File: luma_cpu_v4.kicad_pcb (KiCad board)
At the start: 4 copper layers, 55.8 x 64.2 mm, 117 parts, among them J1 HDMI_A_1.4, J2 USB_C_Receptacle_PowerOnly_6P, J3 Conn_02x03_Odd_Even, J4 USB_A, Q2 DMG2301L, SW1 SW_SPDT, U1 LFE5U-xxF-xBG381I, U10 TPD1E05U06DYA, U11 W25Q128JVS, U12 USB3300-EZK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

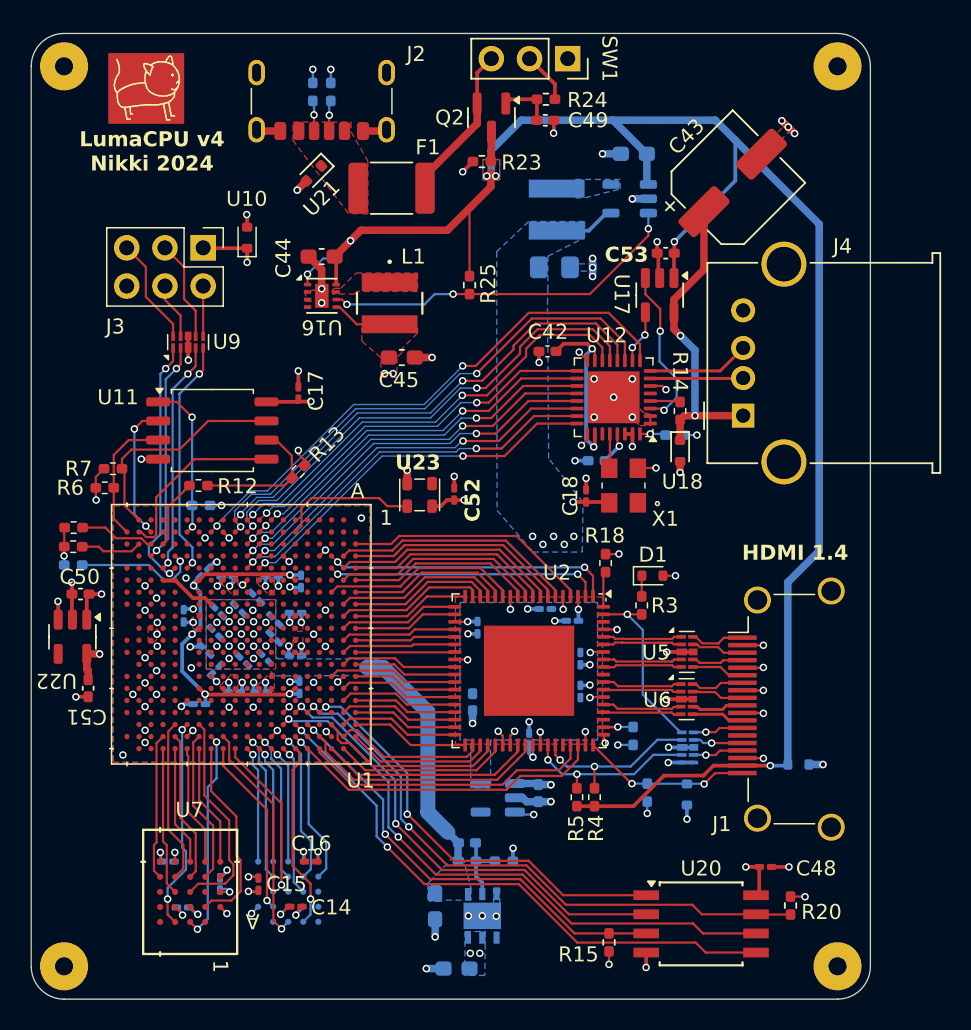
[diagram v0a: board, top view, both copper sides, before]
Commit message: added some capacitors to various components that weren't capacitored enough
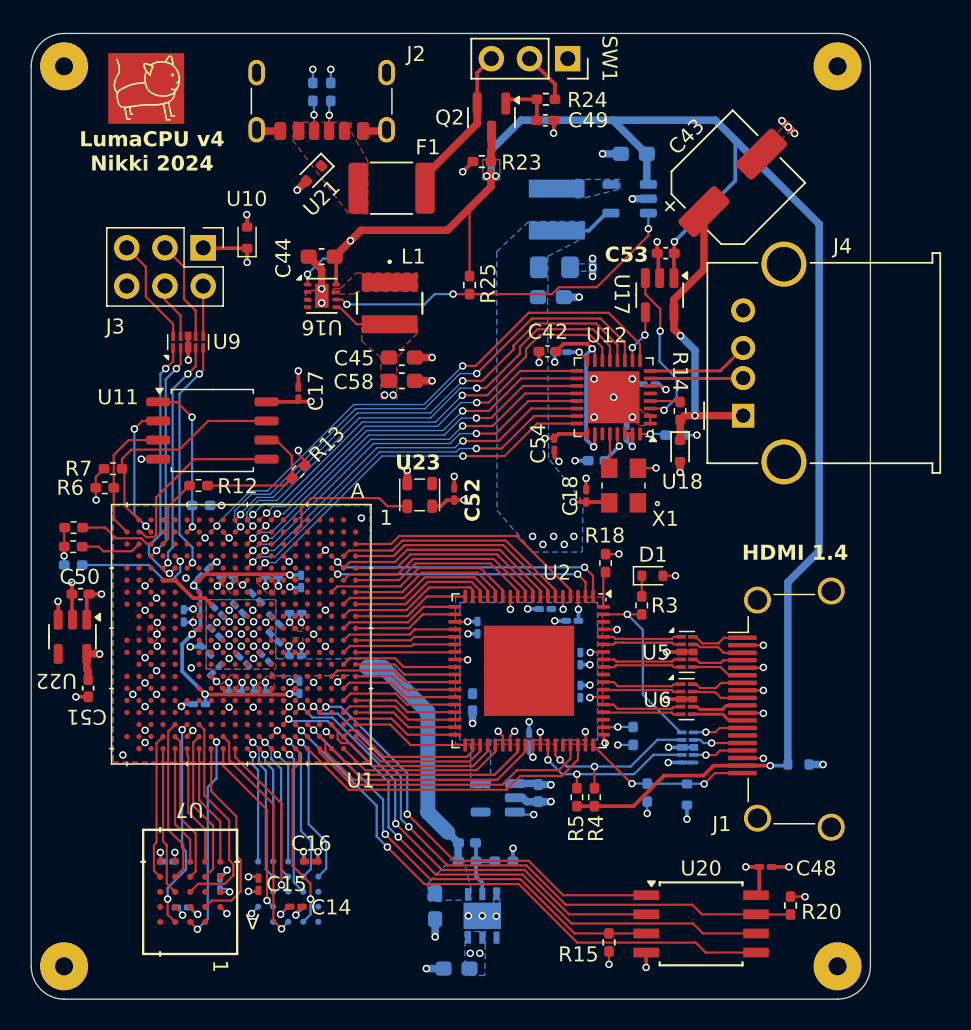
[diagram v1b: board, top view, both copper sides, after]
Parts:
- added C54: 220nF, Capacitor_SMD:C_0201_0603Metric_Pad0.64x0.40mm_HandSolder, F.Cu at (116.0, 89.1)
- added C55: 220nF, Capacitor_SMD:C_0201_0603Metric_Pad0.64x0.40mm_HandSolder, B.Cu at (116.4, 82.9)
- added C56: 220nF, Capacitor_SMD:C_0201_0603Metric_Pad0.64x0.40mm_HandSolder, B.Cu at (122.3, 85.1)
- added C57: 220nF, Capacitor_SMD:C_0201_0603Metric_Pad0.64x0.40mm_HandSolder, B.Cu at (120.8, 88.2)
- added C58: 10uF, Capacitor_SMD:C_0603_1608Metric_Pad1.08x0.95mm_HandSolder, F.Cu at (105.9, 84.8)
- added C59: 10uF, Capacitor_SMD:C_0603_1608Metric_Pad1.08x0.95mm_HandSolder, B.Cu at (115.8, 79.3)
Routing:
- net GND: track 89.7 -> 95.0 mm, vias 131 -> 135
- net +3V3: track 30.3 -> 34.7 mm
